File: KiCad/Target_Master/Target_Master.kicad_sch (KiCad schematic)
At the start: 16 parts, among them J1 RJ11 Header, J3 Null_Modem (DB9), U2 PIC16F1788-IP, U3 MAX232

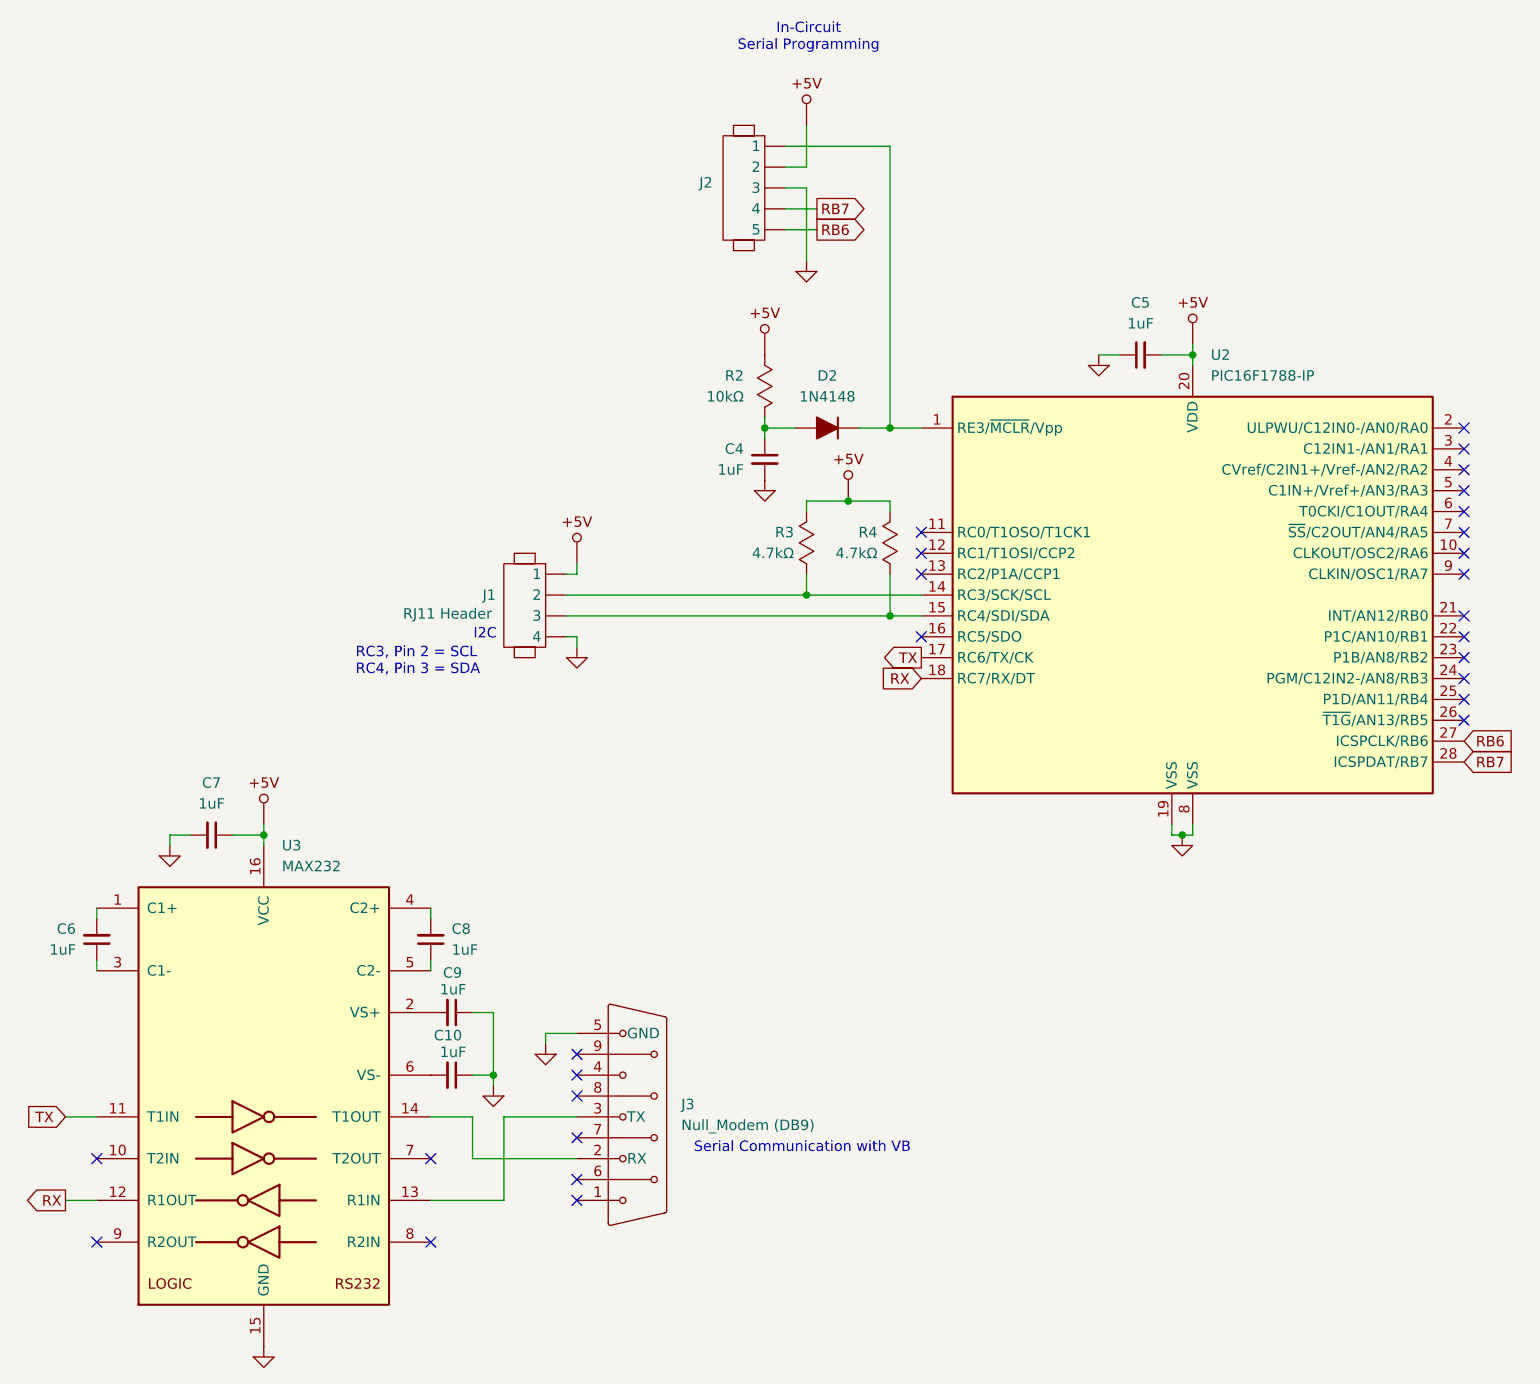
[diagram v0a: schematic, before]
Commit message: adding/fixing UART in master schematic.
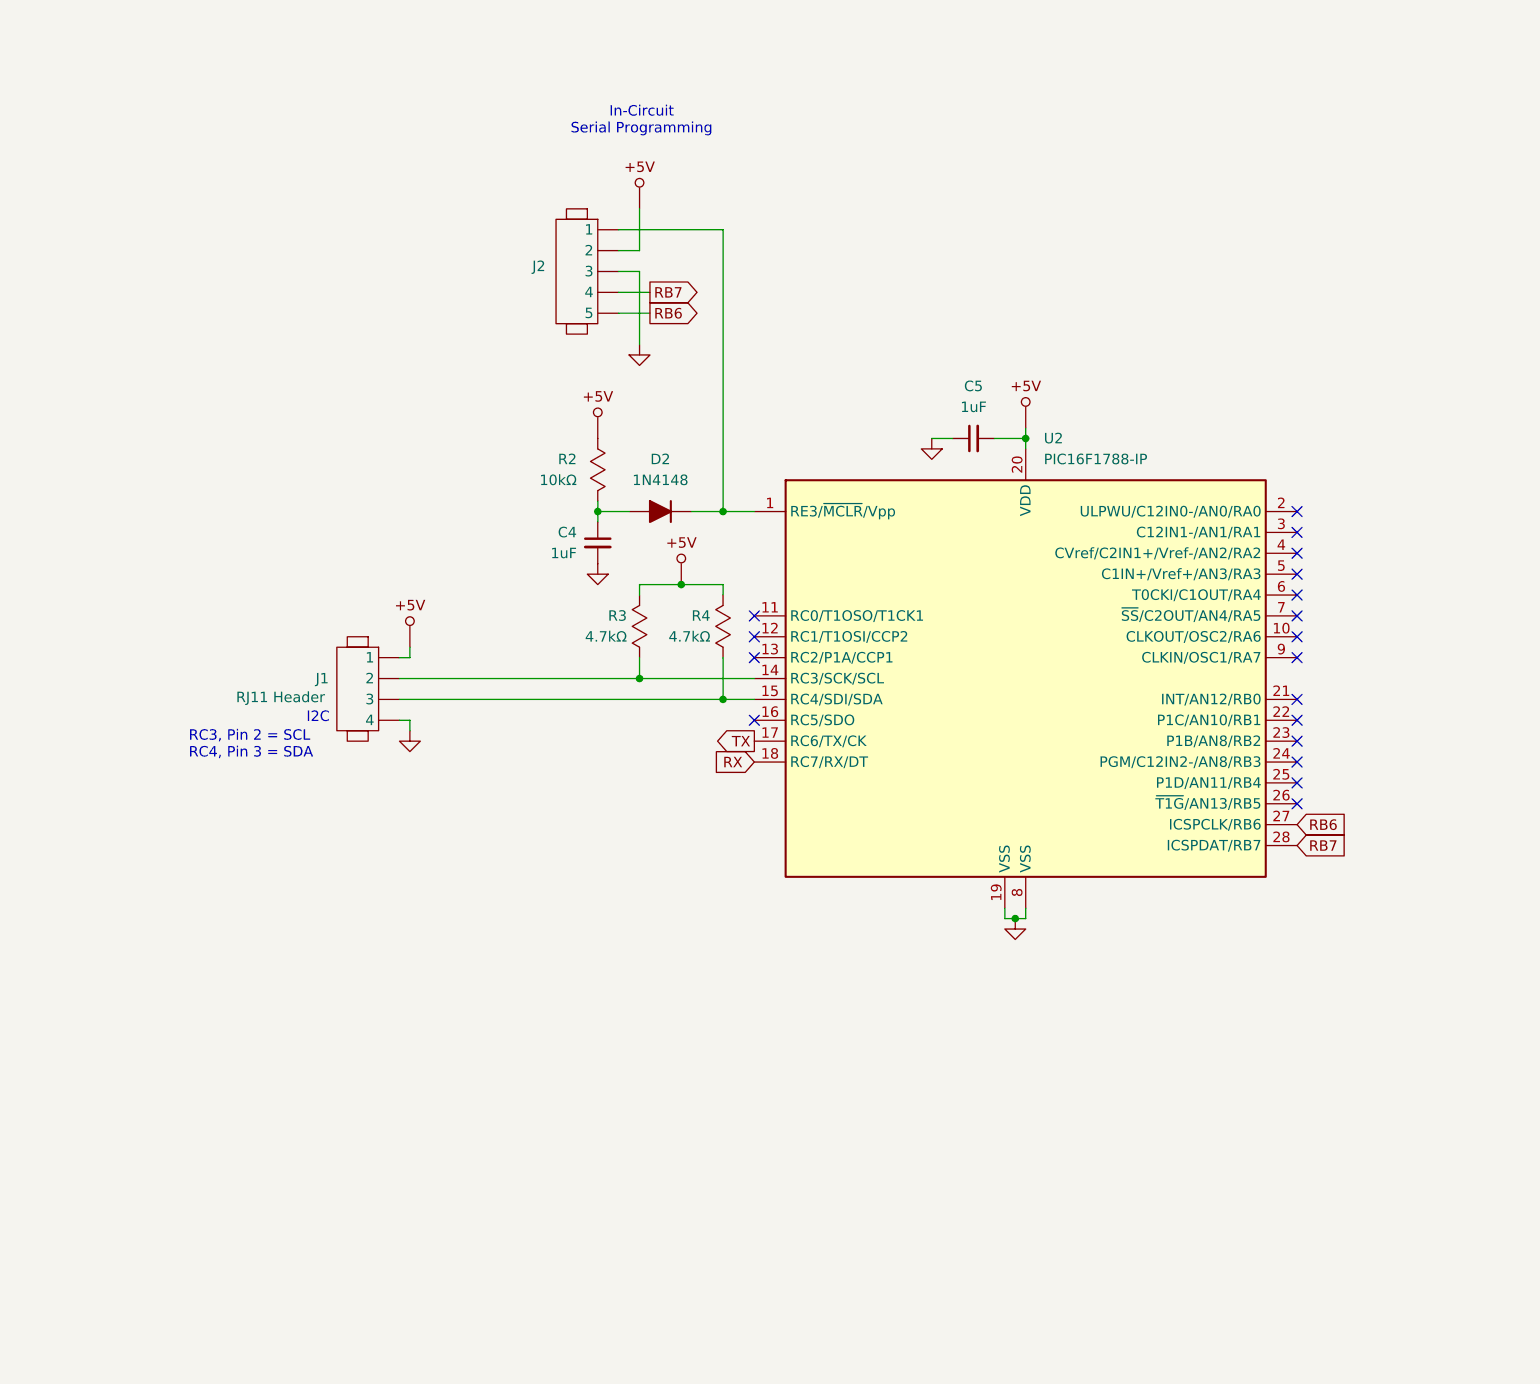
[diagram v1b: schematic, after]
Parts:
- removed C10, C6, C7, C8, C9: 1uF, symbol Device:C_Small
- removed J3: Null_Modem (DB9), symbol Libraries:Null_Modem
- removed U3: MAX232, symbol Interface_UART:MAX232
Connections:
- no-connect marks 28 -> 18
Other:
- note removed: "Serial Communication with VB"
- moved on the sheet: C4, C5, D2, J1, J2, R2, R3, R4, U2
